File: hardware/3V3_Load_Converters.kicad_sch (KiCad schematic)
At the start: 73 parts, among them J23 61300311121, J24 61300311121, Q26 SI2302DDS-T1-GE3, Q27 SI2302DDS-T1-GE3, Q28 EPC2016C, Q29 EPC2016C, Q30 EPC2016C, Q31 EPC2016C, U30 LTC3833EUDC-TRPBF, U31 LTC3833EUDC-TRPBF, U4 INA199C1DCKR

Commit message: commit
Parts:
- removed R29: 5m, symbol Device:R_US
- removed R31, R32: 2.2R, symbol Device:R_US
- removed R39, R40: 100k, symbol Device:R_US
- removed R41, R42, R43, R44, R45, R46: 10R, symbol Device:R_US
- removed R47, R48: 8m, symbol Device:R_US
- removed R49, R51, R53, R55: 0.0R, symbol Device:R_US
- added R30: 5m, footprints:WSL20105L000FEA, symbol WSL20105L000FEA:WSL20105L000FEA
- added R39 (x2): 100k, footprints:CRCW0603100KFKEAHP, symbol CRCW0603100KFKEAHP:CRCW0603100KFKEAHP
- added R41 (x6): 10R, footprints:CRCW060310R0FKEAHP, symbol CRCW060310R0FKEAHP:CRCW060310R0FKEAHP
- added R47 (x2): 8m, footprints:WSL20108L000FEA18, symbol WSL20108L000FEA18:WSL20108L000FEA18
- added R76 (x4): 0.0R, footprints:CRCW06030000Z0EAHP, symbol CRCW06030000Z0EAHP:CRCW06030000Z0EAHP
- added R95, R96: 2.2R, footprints:CRCW06032R20FKEAHP, symbol CRCW06032R20FKEAHP:CRCW06032R20FKEAHP
- R33, R34: footprint (none) -> footprints:CRCW0603100KFKEAHP; symbol Device:R_US -> CRCW0603100KFKEAHP:CRCW0603100KFKEAHP; Arrow Part Number (none) -> CRCW0603100KFKEAHP; Arrow Price/Stock (none) -> https://www.arrow.com/en/products/crcw0603100kfkeahp/vishay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; Height (none) -> 0.55; Manufacturer_Name (none) -> Vishay; Manufacturer_Part_Number (none) -> CRCW0603100KFKEAHP; Mouser Part Number (none) -> 71-CRCW0603100KFKEAH; Mouser Price/Stock (none) -> https://www.mouser.co.uk/ProductDetail/Vishay-Dale/CRCW0603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
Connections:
- net 3V3: now also R41.1, R41.1, R47.1, R47.1, R76.1, R76.1
- net 3V3_A_~{EN}: now also R34.2; no longer R34.1
- net 3V3_B_~{EN}: now also R33.1; no longer R33.2
- net 3V3_VCC1: now also R39.2
- net 3V3_VCC2: now also R39.2
- net GND: now also R34.1; no longer R34.2
- net VBUS: now also R30.1
- net VBUS_BK3V3: now also R33.2, R30.2, R95.2, R96.2; no longer R33.1
- net at U30.16 (BOOST): now also R41.2
- net at C20.1, D13.1 (K): now also R41.1
- net at L2.2: now also R41.1, R47.2 (x2)
- net at C32.2, R50.2, U30.2 (VOSNS+): now also R76.1
- net at C19.1, U31.18 (SENSE+): now also R41.2
- net at C19.2, U31.19 (SENSE-): now also R41.2
- net at C10.2, U30.10 (VIN): now also R96.1
- net at C18.1, U30.18 (SENSE+): now also R41.2
- net at C18.2, U30.19 (SENSE-): now also R41.2
- net at C33.2, R54.2, U31.2 (VOSNS+): now also R76.1
- net at R56.1: now also R76.2
- net at C21.1, D14.1 (K): now also R41.1
- net at R54.1: now also R76.2
- net at U31.16 (BOOST): now also R41.2
- net at C11.2, U31.10 (VIN): now also R95.1
- net at U31.17 (PGOOD): now also R39.1
- net at U30.17 (PGOOD): now also R39.1
- net at R50.1: now also R76.2
- net at R52.1: now also R76.2
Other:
- moved on the sheet: R33, R34

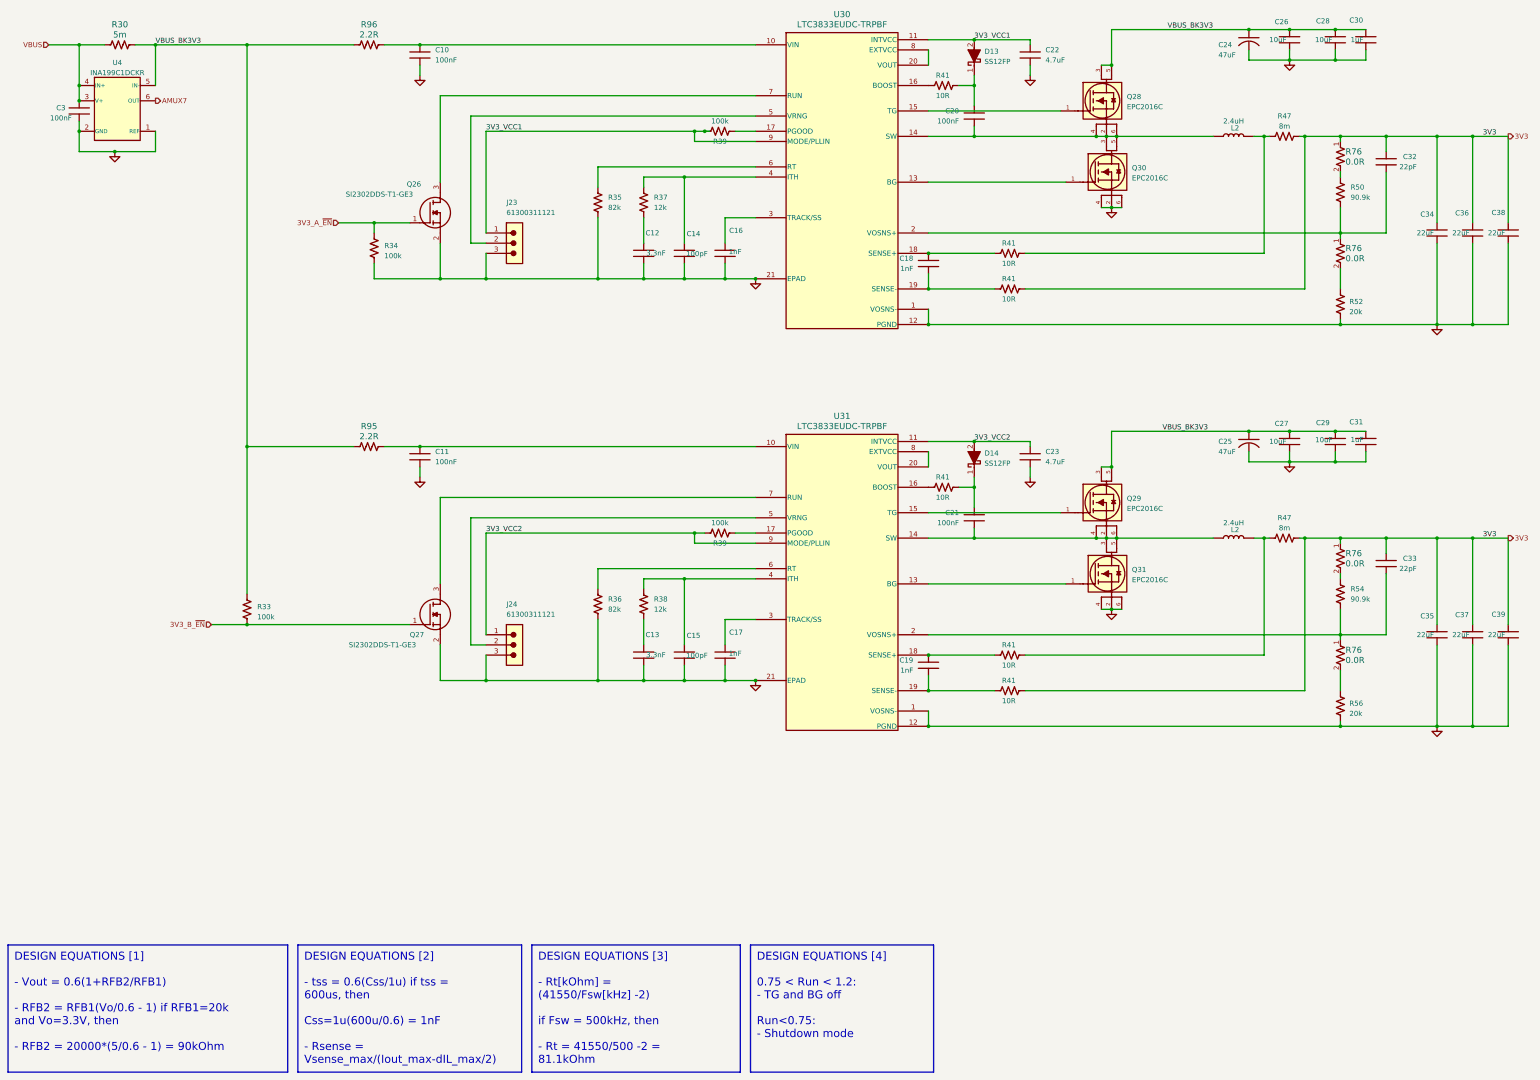
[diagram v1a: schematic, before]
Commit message: hardware: update in footprints
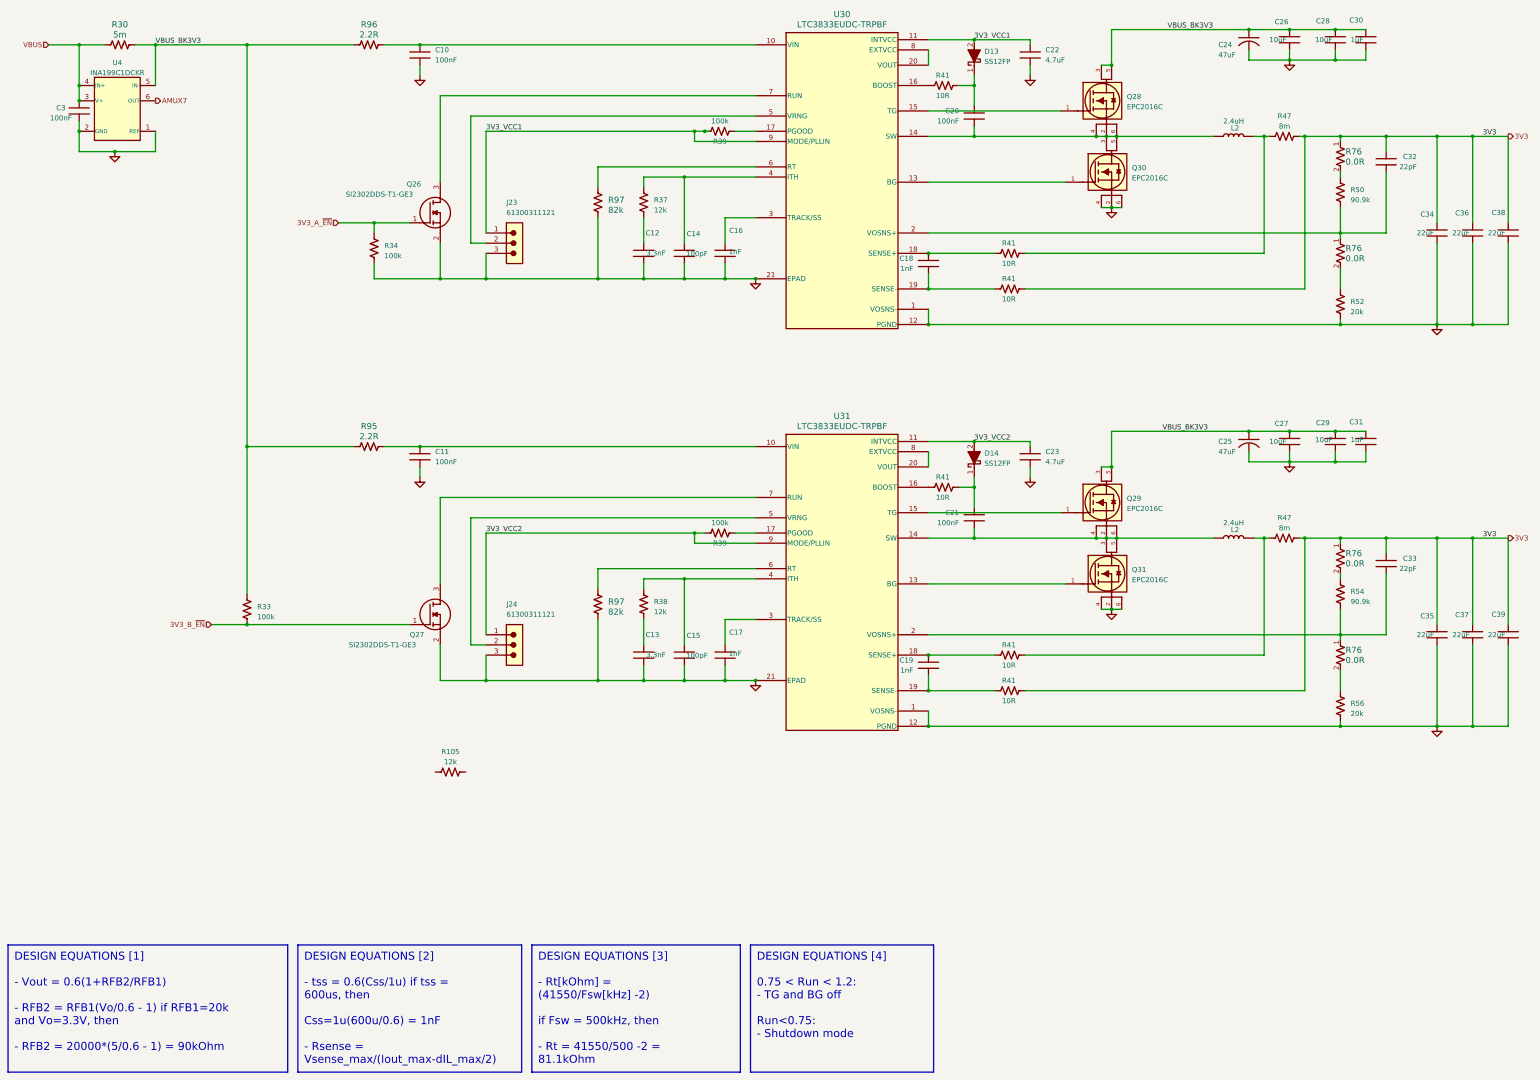
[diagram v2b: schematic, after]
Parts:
- removed R35, R36: 82k, symbol Device:R_US
- added R105: 12k, footprints:CRCW060312K0FKEAHP, symbol CRCW060312K0FKEAHP:CRCW060312K0FKEAHP
- added R97 (x2): 82k, footprints:CRCW060382K0FKEA, symbol CRCW060382K0FKEA:CRCW060382K0FKEA
- R37, R38: footprint (none) -> footprints:CRCW060312K0FKEAHP; symbol Device:R_US -> CRCW060312K0FKEAHP:CRCW060312K0FKEAHP; automotive (none) -> Yes; automotive grade (none) -> Grade 0; category (none) -> Res; composition (none) -> Thick Film; device class L1 (none) -> Passive Components; device class L2 (none) -> Resistors; device class L3 (none) -> Chip SMD Resistors; height (none) -> 0.55mm; ipc land pattern name (none) -> RESC16085X45; lead free (none) -> Yes; library id (none) -> e050c09dfdbc8558; manufacturer (none) -> Vishay; package (none) -> 0603; power (none) -> 250mW; power rating (none) -> 0.33W; resistance (none) -> 12kΩ; rohs (none) -> Yes; series (none) -> CRCW-HP e3; temperature coefficient (none) -> 100ppm/°C; temperature range high (none) -> +155°C; temperature range low (none) -> -55°C; tolerance (none) -> 1%; voltage rating (none) -> 75V
- R50, R54: footprint (none) -> footprints:CRCW060390K9FKEAHP; symbol Device:R_US -> CRCW060390K9FKEAHP:CRCW060390K9FKEAHP; automotive (none) -> Yes; automotive grade (none) -> Grade 0; category (none) -> Res; composition (none) -> Thick Film; device class L1 (none) -> Passive Components; device class L2 (none) -> Resistors; device class L3 (none) -> Chip SMD Resistors; height (none) -> 0.55mm; ipc land pattern name (none) -> RESC16085X45; lead free (none) -> Yes; library id (none) -> 12344a549d2950d0; manufacturer (none) -> Vishay; package (none) -> 0603; power (none) -> 250mW; power rating (none) -> 0.33W; resistance (none) -> 90.9kΩ; rohs (none) -> Yes; series (none) -> CRCW-HP e3; temperature coefficient (none) -> 100ppm/°C; temperature range high (none) -> +155°C; temperature range low (none) -> -55°C; tolerance (none) -> 1%; voltage rating (none) -> 75V
- R52, R56: footprint (none) -> footprints:CRCW060320K0FKEAHP; symbol Device:R_US -> CRCW060320K0FKEAHP:CRCW060320K0FKEAHP; automotive (none) -> Yes; automotive grade (none) -> Grade 0; category (none) -> Res; composition (none) -> Thick Film; device class L1 (none) -> Passive Components; device class L2 (none) -> Resistors; device class L3 (none) -> Chip SMD Resistors; height (none) -> 0.55mm; ipc land pattern name (none) -> RESC16085X45; lead free (none) -> Yes; library id (none) -> 6d0e00b833a89e4b; manufacturer (none) -> Vishay; package (none) -> 0603; power (none) -> 250mW; power rating (none) -> 0.33W; resistance (none) -> 20kΩ; rohs (none) -> Yes; series (none) -> CRCW-HP e3; temperature coefficient (none) -> 100ppm/°C; temperature range high (none) -> +155°C; temperature range low (none) -> -55°C; tolerance (none) -> 1%; voltage rating (none) -> 75V
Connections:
- net GND: now also R52.1, R56.1, R97.1, R97.1; no longer R52.2, R56.2
- net at C32.2, R76.1, U30.2 (VOSNS+): now also R50.1; no longer R50.2
- net at R54.1: now also C33.2, R76.1, U31.2 (VOSNS+); no longer R76.2
- net at R76.2: now also R50.2; no longer R50.1
- net at R76.2: now also R52.2; no longer R52.1
- net at C15.1, U31.4 (ITH): now also R38.2; no longer R38.1
- net at U31.6 (RT): now also R97.2
- net at R76.2: now also R56.2; no longer R56.1
- net at U30.6 (RT): now also R97.2
- net at C13.1: now also R38.1; no longer R38.2
- new net: R54.2, R76.2
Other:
- moved on the sheet: R37, R38, R50, R52, R54, R56
